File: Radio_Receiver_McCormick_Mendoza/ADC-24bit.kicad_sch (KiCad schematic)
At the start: 28 parts, among them J21 SDR Out, J22 Q_OUT, J30 Q_OUT, J31 Q_OUT, J32 Q_OUT, J7 I_OUT, U10 OPA1612AxD, U12 PCM1808PWR

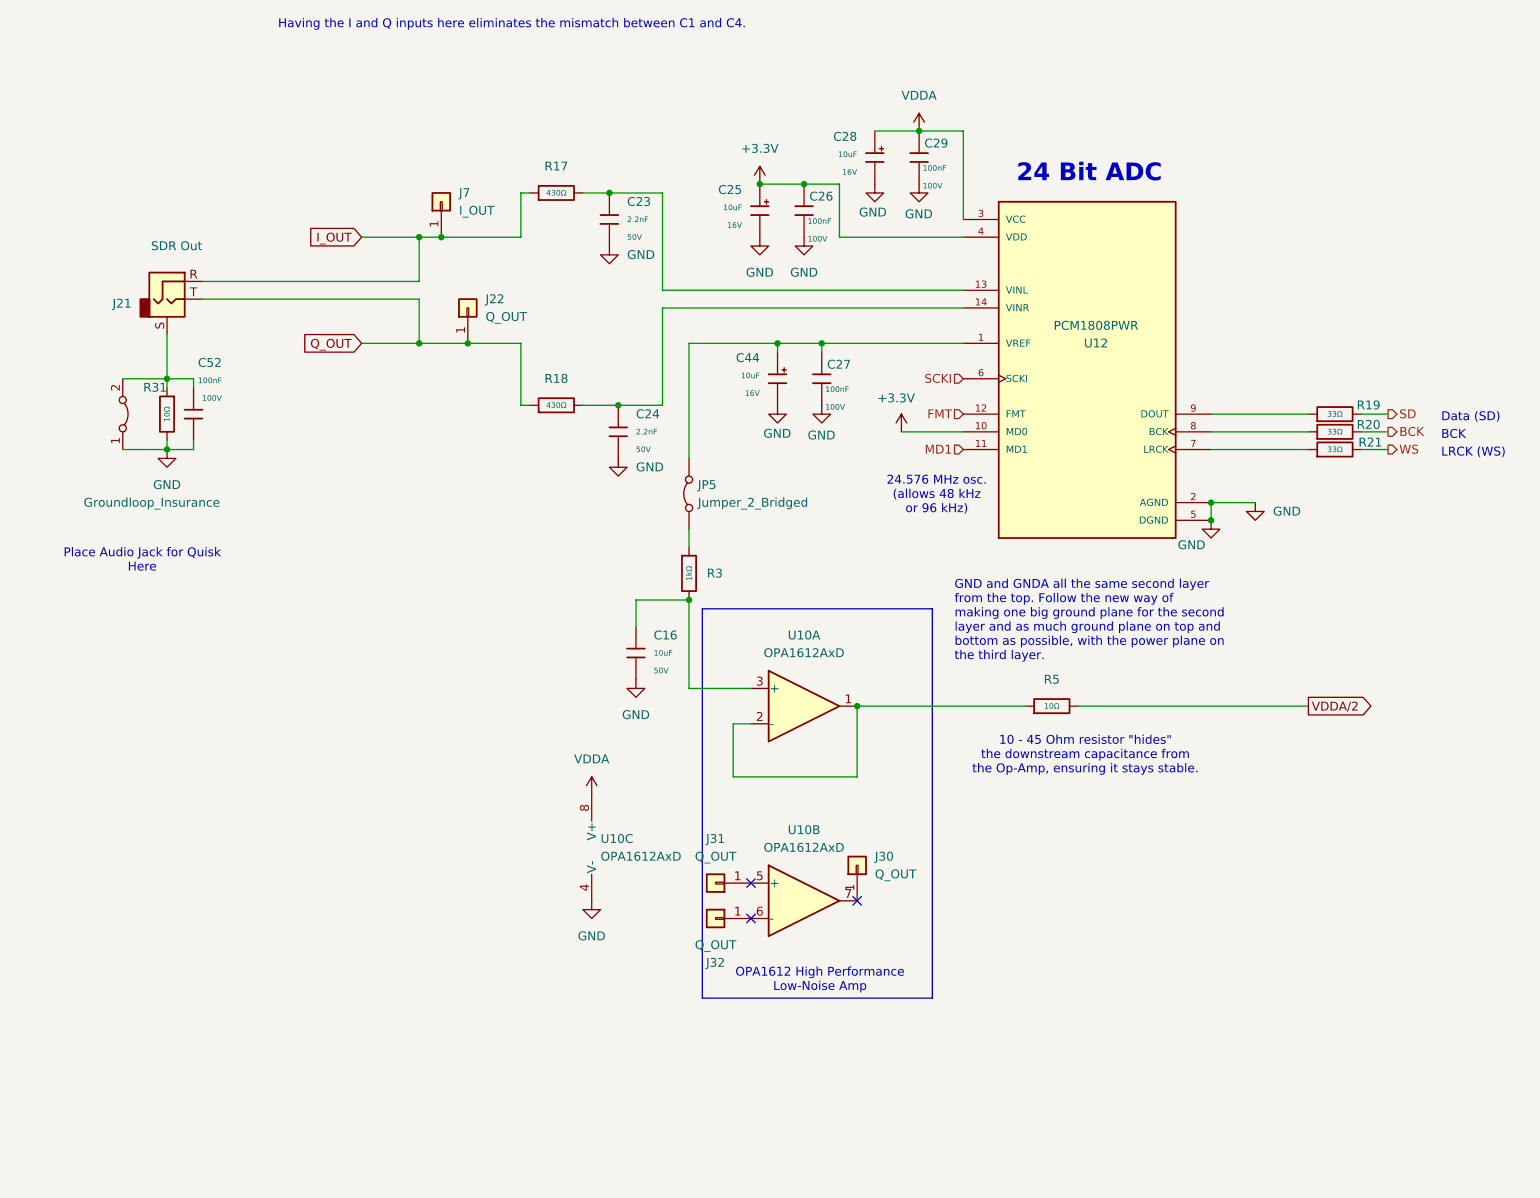
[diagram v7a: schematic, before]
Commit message: Integrated signal path modules
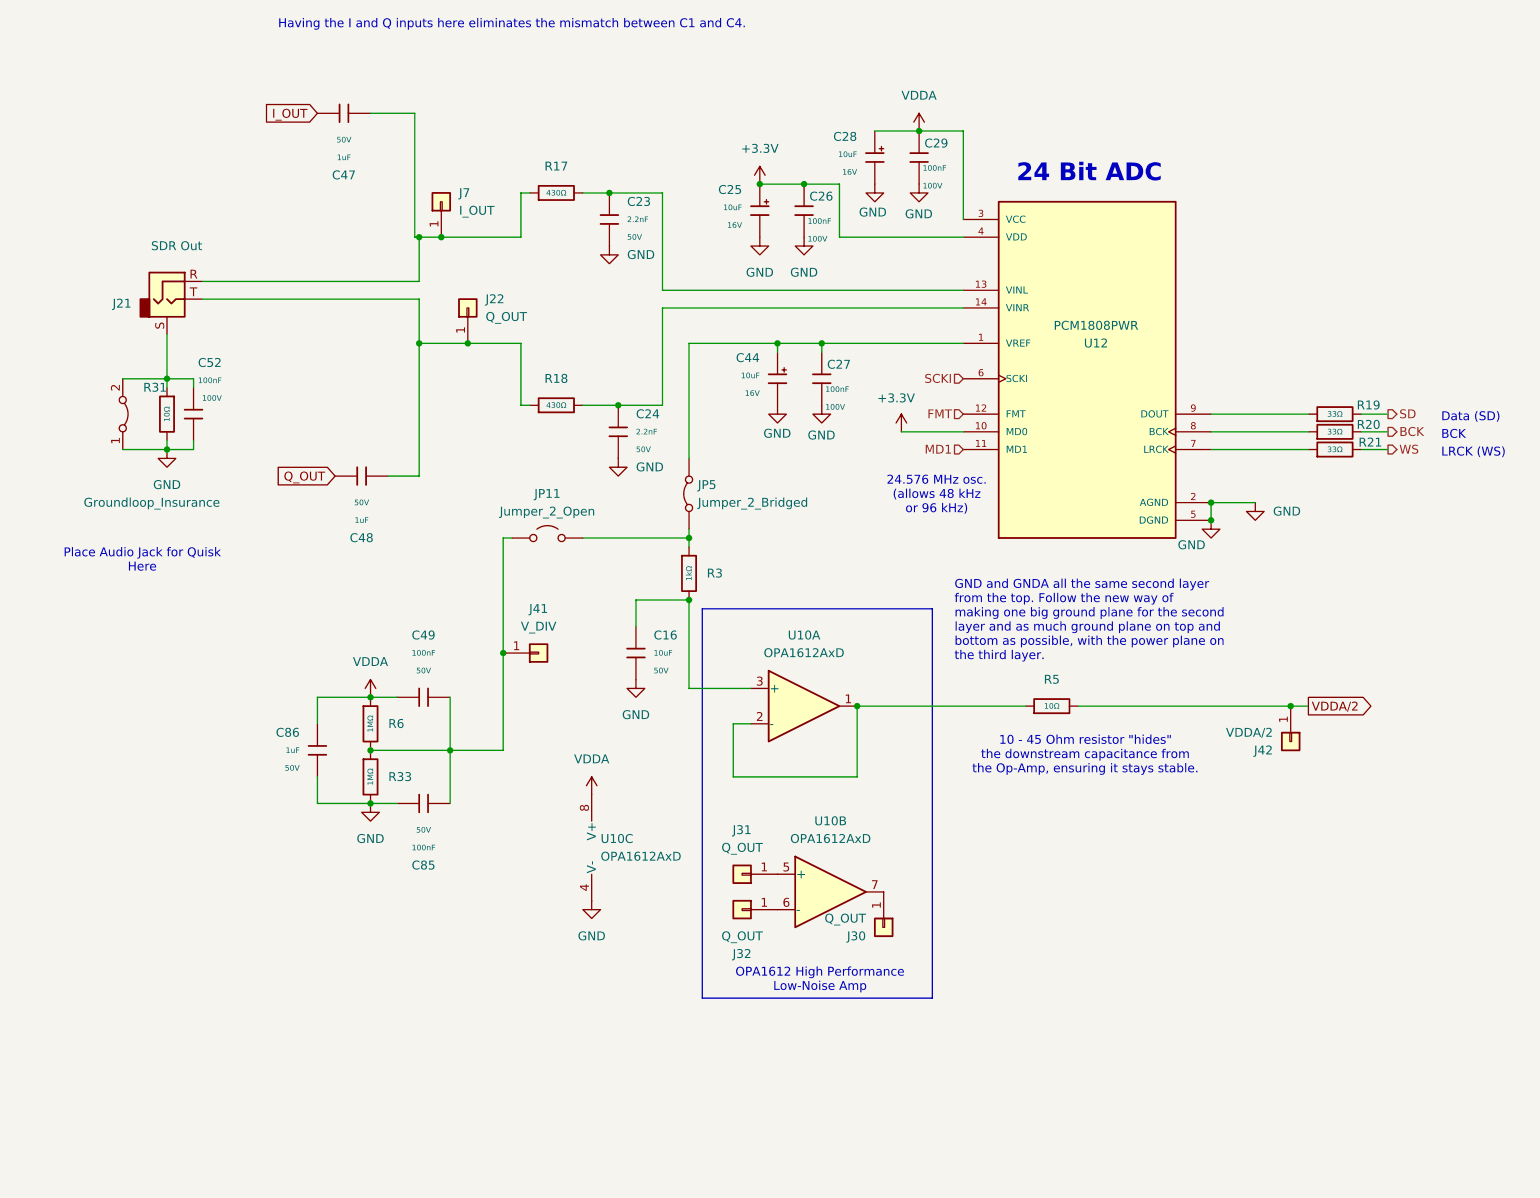
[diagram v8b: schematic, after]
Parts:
- added C47, C48: 1uF, PCM_JLCPCB:C_0805, symbol PCM_JLCPCB-Capacitors:0805,1uF
- added C49, C85: 100nF, PCM_JLCPCB:C_0402, symbol PCM_JLCPCB-Capacitors:0402,100nF,(2)
- added C86: 1uF, PCM_JLCPCB:C_0603, symbol PCM_JLCPCB-Capacitors:0603,1uF
- added J41: V_DIV, Connector_PinHeader_2.54mm:PinHeader_1x01_P2.54mm_Vertical, symbol Connector_Generic:Conn_01x01
- added J42: VDDA/2, Connector_PinHeader_2.54mm:PinHeader_1x01_P2.54mm_Vertical, symbol Connector_Generic:Conn_01x01
- added JP11: Jumper_2_Open, symbol Jumper:Jumper_2_Open
- added R33, R6: 1MΩ, PCM_JLCPCB:R_0603, symbol PCM_JLCPCB-Resistors:0603,1MΩ
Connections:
- net GND: now also C85.1, C86.2, R33.2
- net I_OUT: now also C47.2; no longer J21.R, J7.1 (Pin_1), R17.1
- net Q_OUT: now also C48.2; no longer J21.T, J22.1 (Pin_1), R18.1
- net VDDA: now also C49.2, C86.1, R6.1
- net VDDA/2: now also J42.1 (Pin_1)
- net at JP5.1 (A), R3.1: now also JP11.2 (B)
- new net: C49.1, C85.2, J41.1 (Pin_1), JP11.1 (A), R33.1, R6.2
- new net: C48.1, J21.T, J22.1 (Pin_1), R18.1
- new net: C47.1, J21.R, J7.1 (Pin_1), R17.1
- no-connect marks 3 -> 0
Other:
- moved on the sheet: J30, J31, J32, U10B
